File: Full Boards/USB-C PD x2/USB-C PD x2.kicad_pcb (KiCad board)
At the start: 4 copper layers, 96 x 136 mm, 162 parts, among them J1 Conn_02x05_Odd_Even, J2 Conn_01x05_Pin

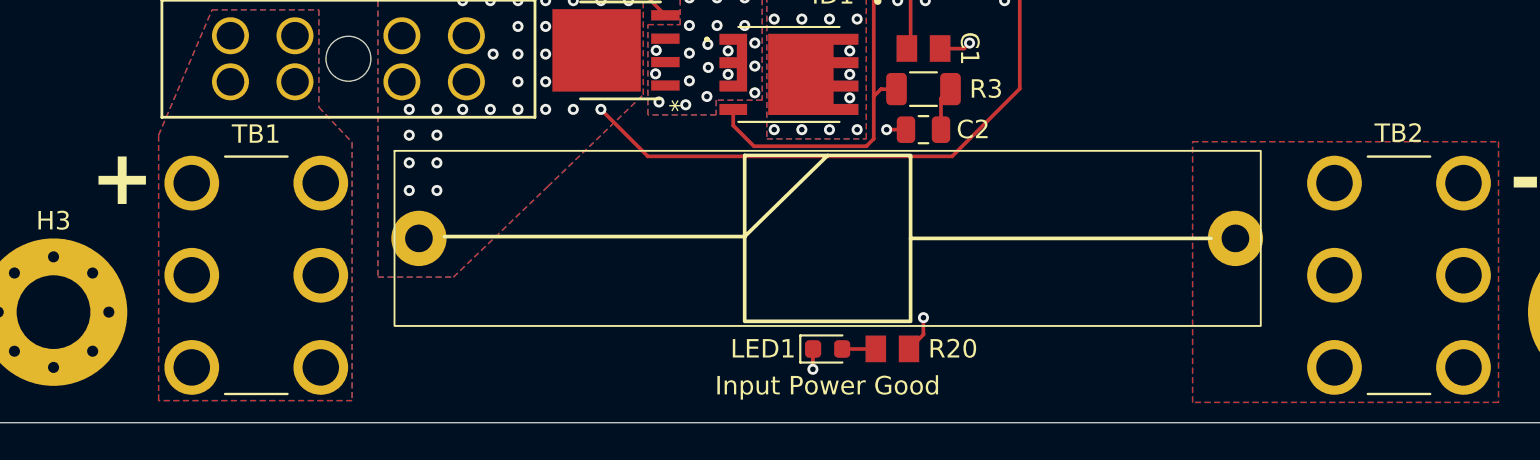
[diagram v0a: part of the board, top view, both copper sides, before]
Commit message: Updated the symbols and footprints for replaced foot prints.
Signed-off-by: digimer <digital.mermaid@gmail.com>
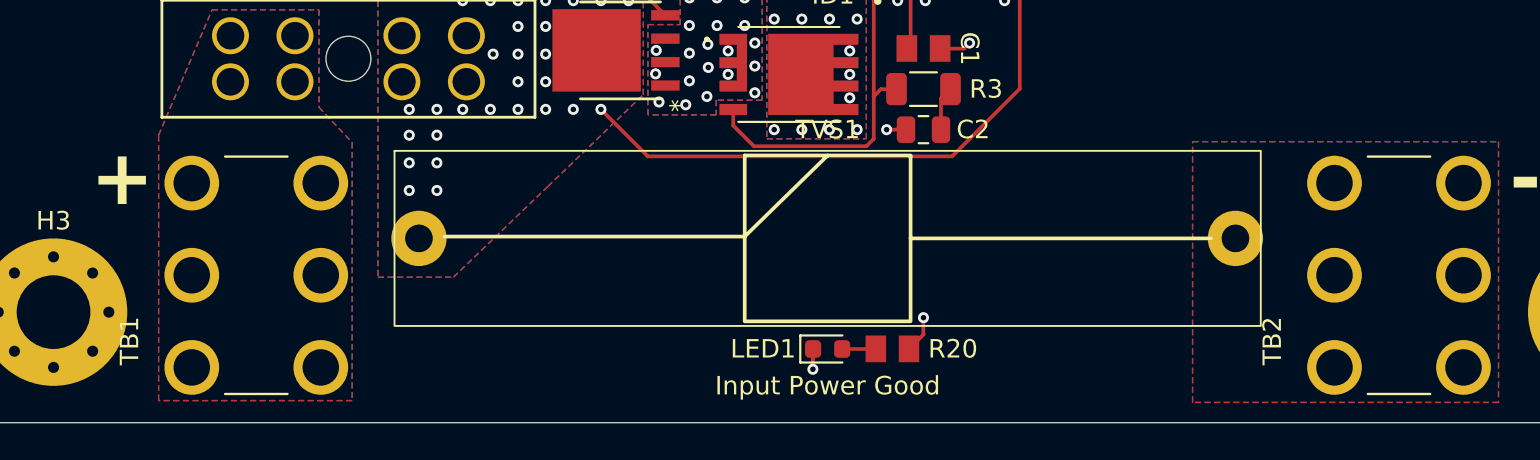
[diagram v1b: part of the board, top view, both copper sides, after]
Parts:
- PR1, PR2: value 4.7KR -> 2.2KR
- TB1, TB2: value Keystone Electronics 7799 -> 7799
- TVS1: footprint mr-stuff:DIOAD4425W136L885D885 -> mr-stuff:Littelfuse SDL

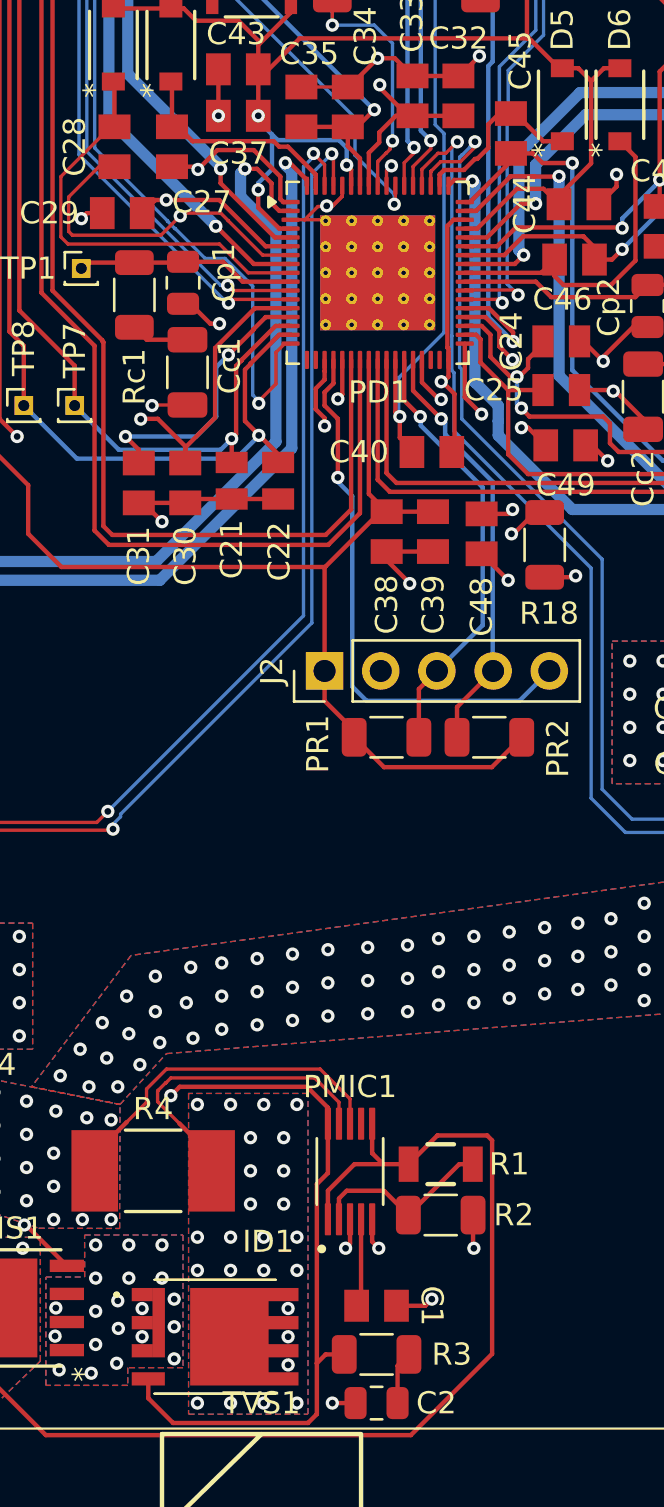
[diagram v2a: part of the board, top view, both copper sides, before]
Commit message: Bumped the Infineon CYPD7272 footprint to use 0.3mm instead of 0.2mm thermal vias.
Signed-off-by: digimer <digital.mermaid@gmail.com>
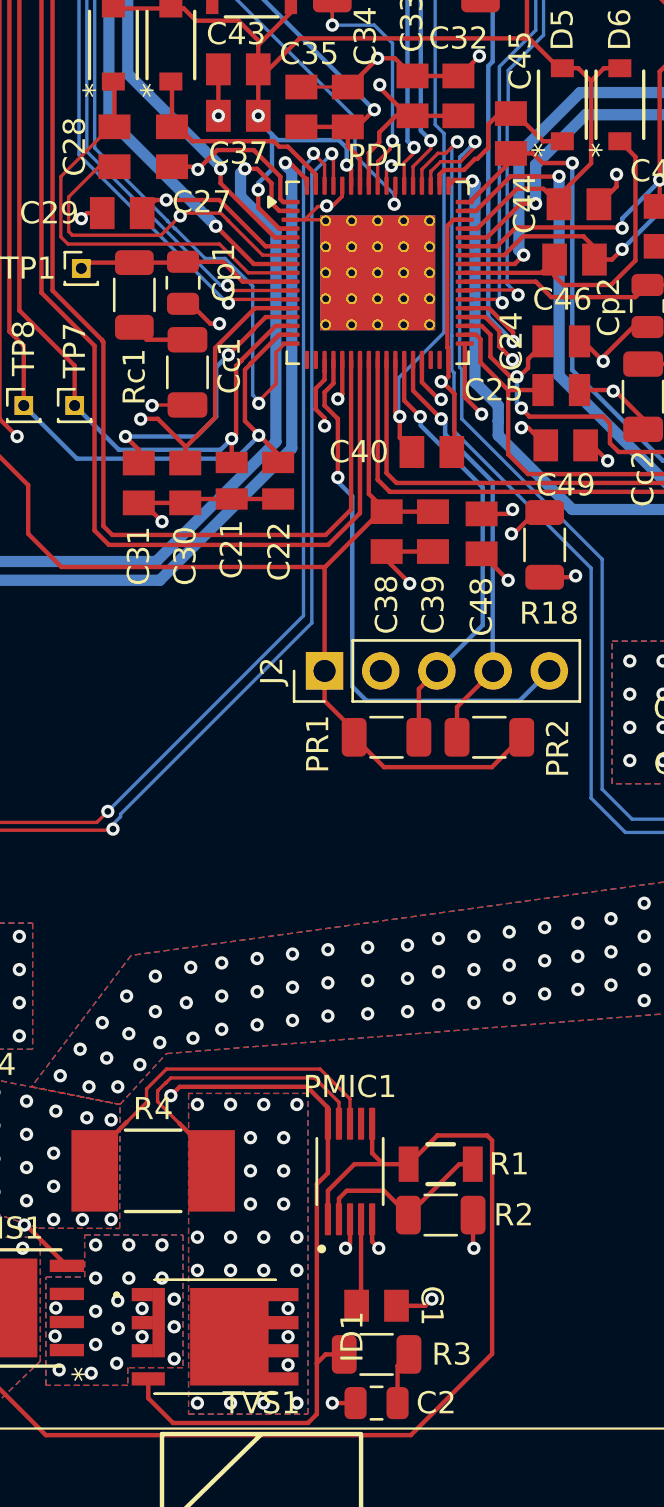
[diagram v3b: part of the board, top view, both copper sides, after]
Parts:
- HS1: value Nexperia PSMN1R4-40YLDX -> PSMN1R4-40YLDX
- ID1: value Infineon IAUC120N04S6L008ATMA1 -> IAUC120N04S6L008ATMA1; footprint mr-stuff:Infineon IAUC120N06S5N017ATMA1 -> mr-stuff:Infineon IAUC120N04S6L008ATMA1
- PD1: footprint Package_DFN_QFN:QFN-68-1EP_8x8mm_P0.4mm_EP5.2x5.2mm_ThermalVias -> mr-stuff:Infineon CYPD727x

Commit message: Changed the current sense resistor on the PMIC to 1.5mR 6W from 2mR 5W to help increase the trip margin.
Signed-off-by: digimer <digital.mermaid@gmail.com>
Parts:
- R4: value 2mR -> 1.5mR; footprint mr-stuff:Vishay WSLP -> mr-stuff:Vishay WSLF2512
- moved R4 0.07 mm to (95.0, 149.6)

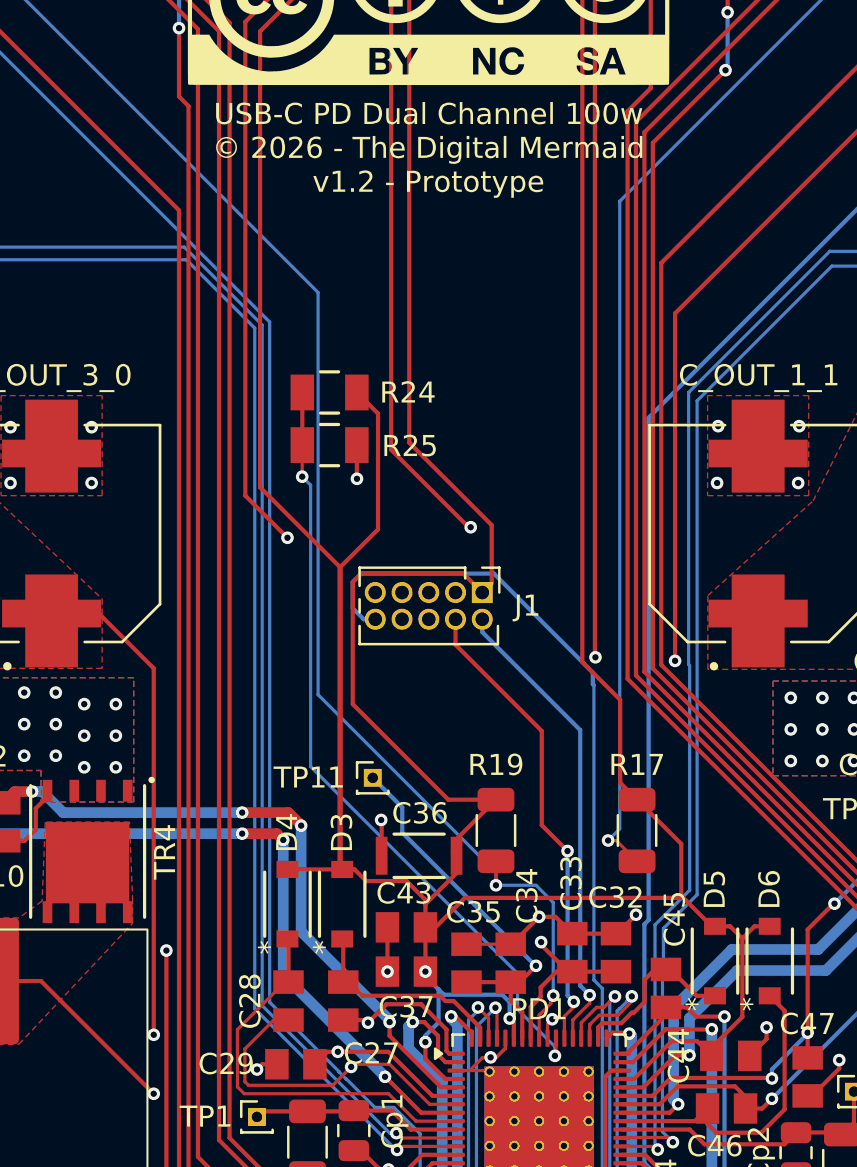
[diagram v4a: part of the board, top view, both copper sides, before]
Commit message: Removed C34 (1uF on CLPD7272 VCCD, pin 62). As per the datasheet; "1.8-V core LDO output. Connect a 0.1-µF bypass capacitor to ground. Do not connect anything else to this pin."
Signed-off-by: digimer <digital.mermaid@gmail.com>
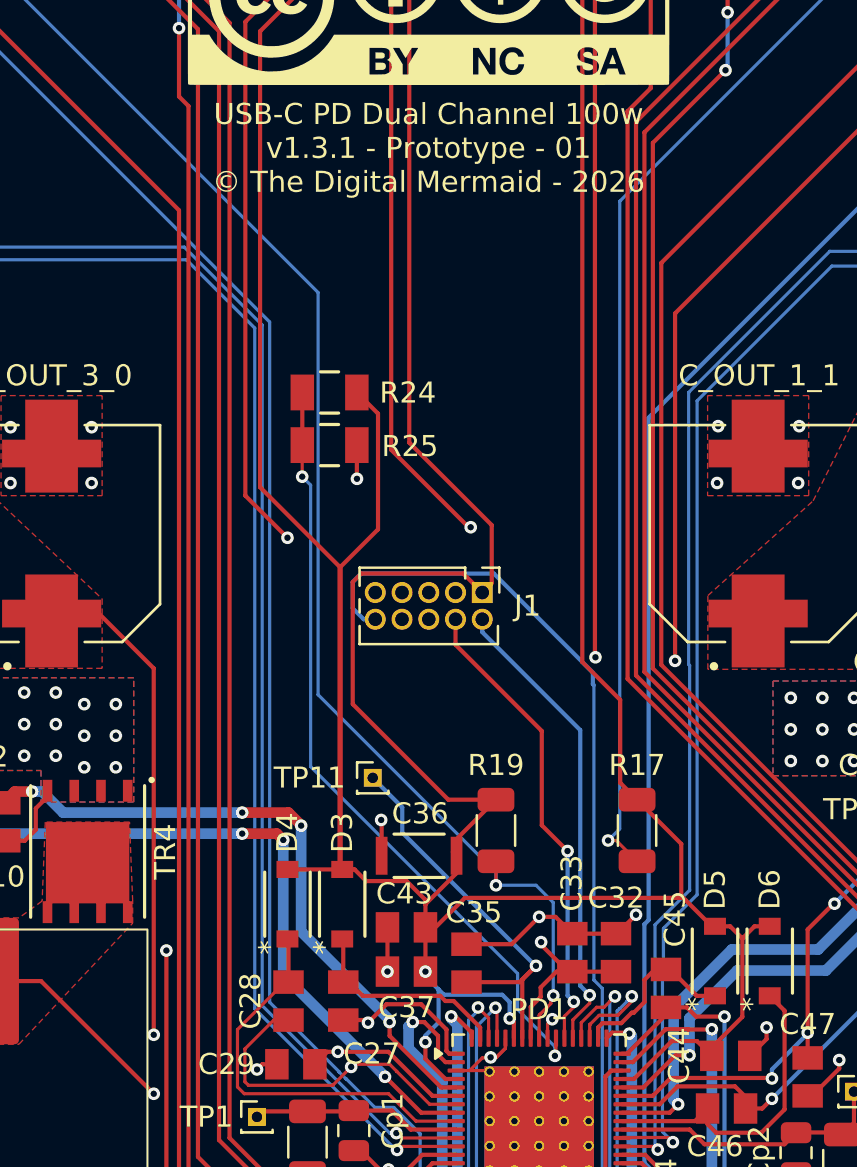
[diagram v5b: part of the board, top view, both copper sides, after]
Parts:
- removed C34: 1μF, mr-stuff:Kyocera AVX 08051A0R8CAT2A
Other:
- board text added: "USB-C PD Dual Channel 100w v1.3.1 - Prototype - 01 © The Digital Mermaid - 2026"
- board text removed: "USB-C PD Dual Channel 100w © 2026 - The Digital Mermaid v1.2 - Prototype"
